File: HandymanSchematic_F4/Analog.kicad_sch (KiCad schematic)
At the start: 36 parts, among them Q1 BC847, U2 TL074, U6 TL072

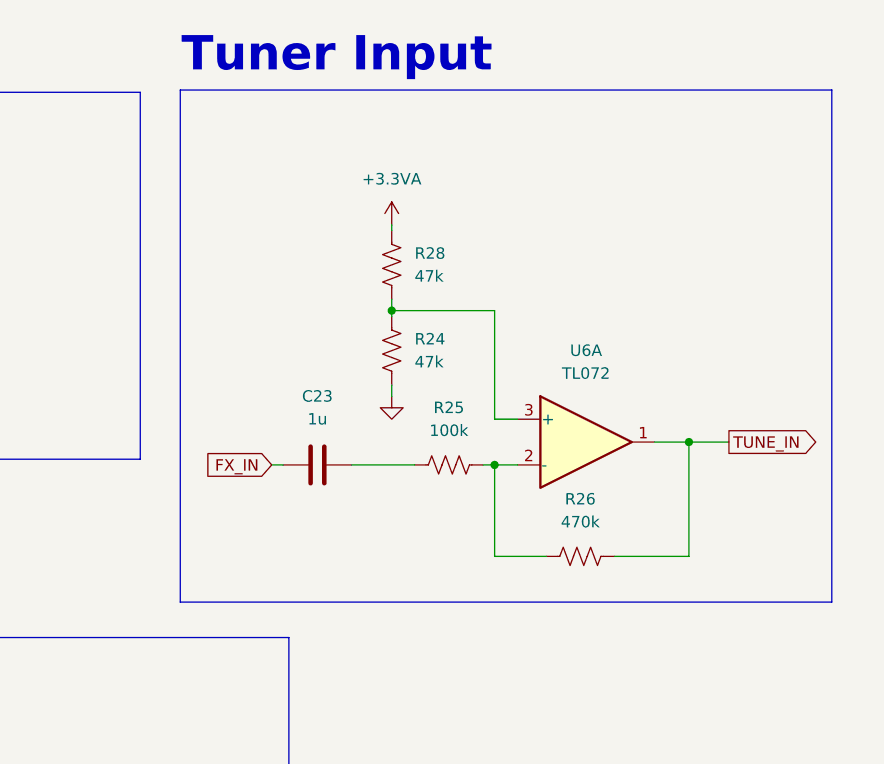
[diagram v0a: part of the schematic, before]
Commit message: schematic changes for DFM
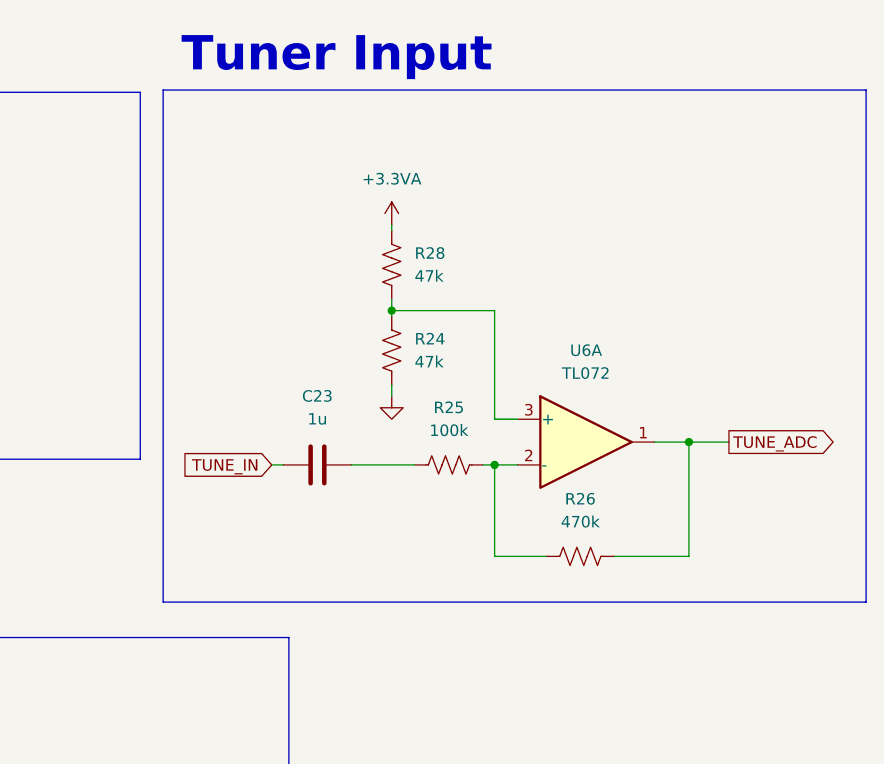
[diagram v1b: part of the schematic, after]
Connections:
- net FX_IN is gone; now on net TUNE_IN: C23.1
- net TUNE_IN: no longer R26.2, U6.1
- new net TUNE_ADC: R26.2, U6.1
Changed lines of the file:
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@@
 	)
 	(rectangle
-		(start 188.595 20.574)
-		(end 260.985 77.47)
+		(start 186.69 20.574)
+		(end 264.795 77.47)
 		(stroke
 			(width 0)
@@
 		)
 	)
-	(global_label "TUNE_IN"
+	(global_label "TUNE_ADC"
 		(shape output)
 		(at 249.555 59.69 0)
@@
 		)
 		(property "Intersheetrefs" "${INTERSHEET_REFS}"
-			(at 260.2207 59.69 0)
+			(at 261.914 59.69 0)
 			(hide yes)
 			(show_name no)
@@
 		)
 	)
-	(global_label "FX_IN"
+	(global_label "TUNE_IN"
 		(shape input)
 		(at 198.755 62.23 180)
@@
 		)
 		(property "Intersheetrefs" "${INTERSHEET_REFS}"
-			(at 190.5688 62.23 0)
+			(at 188.0893 62.23 0)
 			(hide yes)
 			(show_name no)

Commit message: set up BOM w supplier links fixing merge conflict
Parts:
- C1, C3, C4: MPN (none) -> KGF21BR71H104KT; Purchase Link (none) -> https://www.mouser.com/en/ProductDetail/KYOCERA-AVX/KGF21BR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
- C10, C23, C6: MPN (none) -> KGM21AR51E105KU; Purchase Link (none) -> https://www.mouser.com/en/ProductDetail/KYOCERA-AVX/KGM21AR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
- C11: MPN (none) -> KGM21NR71H472JM; Purchase Link (none) -> https://www.mouser.com/en/ProductDetail/KYOCERA-AVX/KGM21NR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
- D1, D4, D5, D6, D7: MPN (none) -> 1N4148W-7-F; Purchase Link (none) -> https://www.mouser.com/en/ProductDetail/Diodes-Incorporated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
- Q1: MPN (none) -> BC847C-C; Purchase Link (none) -> https://www.mouser.com/en/ProductDetail/Diotec-Semiconducto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
- R1, R10, R2, R24, R28, R5, R7: MPN (none) -> RK73B2ATTE473J; Purchase Link (none) -> https://www.mouser.com/en/ProductDetail/KOA-Speer/RK73B2ATT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
- R12, R13, R18, R21, R26, R8: MPN (none) -> AC0805JR-07470KL; Purchase Link (none) -> https://www.mouser.com/en/ProductDetail/YAGEO/AC0805JR-0747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
- R15, R19: MPN (none) -> RT0805FRE0751KL; Purchase Link (none) -> https://www.mouser.com/en/ProductDetail/YAGEO/RT0805FRE0751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
- R22, R25, R9: MPN (none) -> RC0805FR-10100KL; Purchase Link (none) -> https://www.mouser.com/en/ProductDetail/YAGEO/RC0805FR-1010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
- R3: MPN (none) -> AC0805JR-0710KL; Purchase Link (none) -> https://www.mouser.com/en/ProductDetail/YAGEO/AC0805JR-0710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
- RV1, RV2: MPN (none) -> RV9022NO-PA30B7.0-B10K-000-W3.0; Purchase Link (none) -> https://www.taydaelectronics.com/potentiometer-variable-res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
- U2: MPN (none) -> TL074HIDR; Purchase Link (none) -> https://www.mouser.com/en/ProductDetail/Texas-Instruments/T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
- U6: MPN (none) -> TL072HIDR; Purchase Link (none) -> https://www.mouser.com/en/ProductDetail/Texas-Instruments/T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

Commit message: noise schematic tweaks
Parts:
- removed R25: 100k, Resistor_SMD:R_0805_2012Metric, symbol Device:R_US
- removed U6: TL072, Package_SO:SOIC-8_3.9x4.9mm_P1.27mm, symbol Amplifier_Operational:TL072
- added C2, C9: 10u, Capacitor_SMD:C_0805_2012Metric, symbol Device:C
- added C25: 2n2, Capacitor_SMD:C_0805_2012Metric, symbol Device:C
- added D2: BAT54S, Package_TO_SOT_SMD:SOT-23, symbol Diode:BAT54S
- added R11, R4, R6: 220, Resistor_SMD:R_0805_2012Metric, symbol Device:R_US
- added R30: 1Meg, Resistor_SMD:R_0805_2012Metric, symbol Device:R_US
- added R38: 470k, Resistor_SMD:R_0805_2012Metric, symbol Device:R_US
- added R39: 4k7, Resistor_SMD:R_0805_2012Metric, symbol Device:R_US
- added U5: LM2904, Package_SO:SOIC-8_3.9x4.9mm_P1.27mm, symbol Amplifier_Operational:LM2904
- R12, R8: value 470k -> 1Meg
- R13, R26: value 470k -> 100k
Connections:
- net +3.3VA: now also D2.2 (K)
- net AmpAnode: now also R4.2; no longer D7.2 (A)
- net AmpCathode: now also R6.1; no longer D4.1 (K)
- net GND: now also C2.2, C25.2, C9.2, D2.1 (A), U5.4 (V-)
- net TUNE_ADC: now also C25.1, D2.3 (COM), R39.2; no longer R26.2
- net VG: now also U5.6 (-), U5.7
- net at R26.1: now also R38.2, U5.2 (-)
- net at R24.1, R28.2: now also C2.1, R30.2, R38.1
- net at R1.2, R2.1: now also C9.1, U5.5 (+)
- net at C23.2: now also R30.1, U5.3 (+)
- net at R22.2, U2.8: now also R11.1; no longer C10.1
- net +9V renamed +9VA
- net +9VA: now also U5.8 (V+)
- new net: D4.1 (K), R6.2
- new net: D7.2 (A), R4.1
- new net: C10.1, R11.2
- new net: R26.2, R39.1, U5.1
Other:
- moved on the sheet: C1, C10, C11, C23, C3, C6, D4, D5, D6, D7, R1, R10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

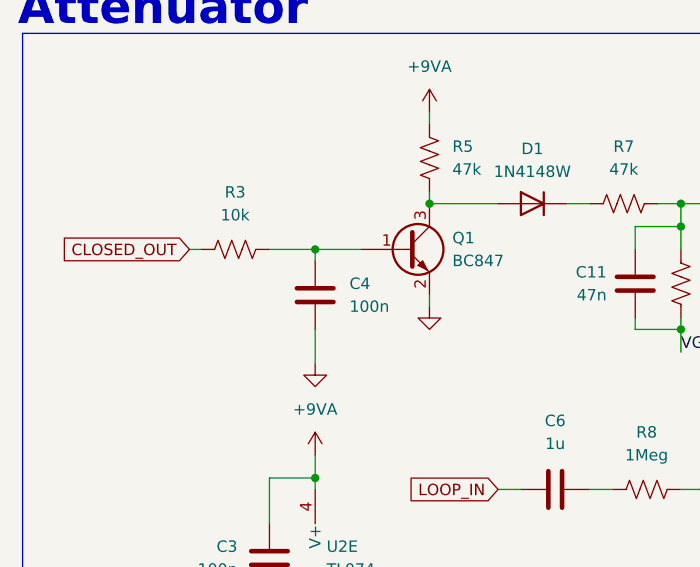
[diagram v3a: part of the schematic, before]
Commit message: switched to FET controlled gate circuit
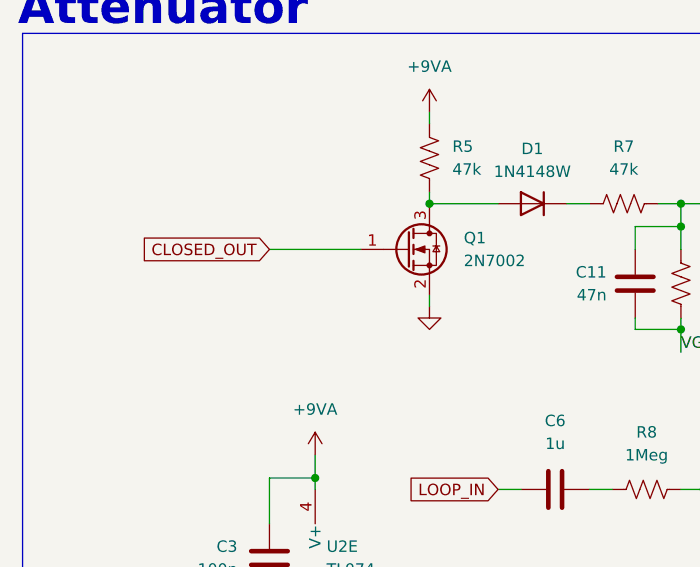
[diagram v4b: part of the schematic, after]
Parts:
- removed C4: 100n, Capacitor_SMD:C_0805_2012Metric, symbol Device:C
- removed Q1: BC847, Package_TO_SOT_SMD:SOT-23, symbol Transistor_BJT:BC847
- removed R3: 10k, Resistor_SMD:R_0805_2012Metric, symbol Device:R_US
- added Q1: 2N7002, Package_TO_SOT_SMD:SOT-23, symbol Transistor_FET:2N7002
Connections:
- net CLOSED_OUT: now also Q1.1 (G)
- net GND: now also Q1.2 (S)
- net at D1.2 (A), R5.2: now also Q1.3 (D)

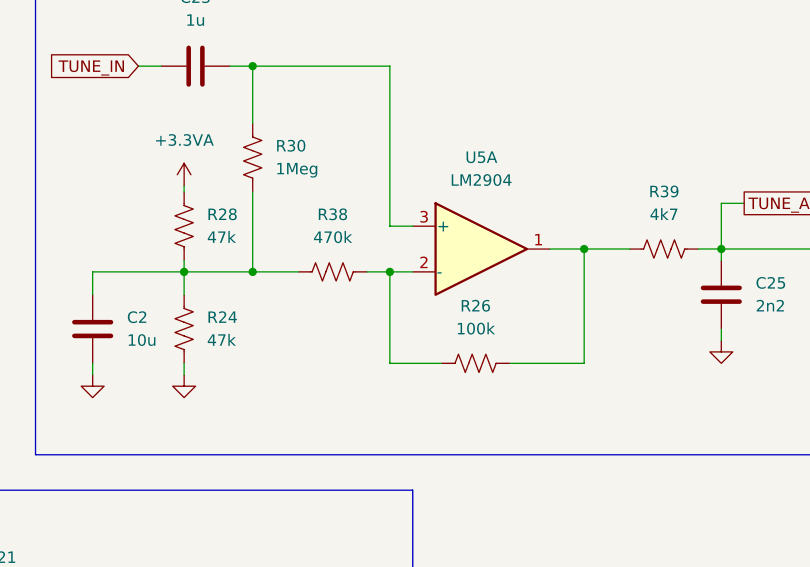
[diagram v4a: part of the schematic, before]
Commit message: fixed hysteresis
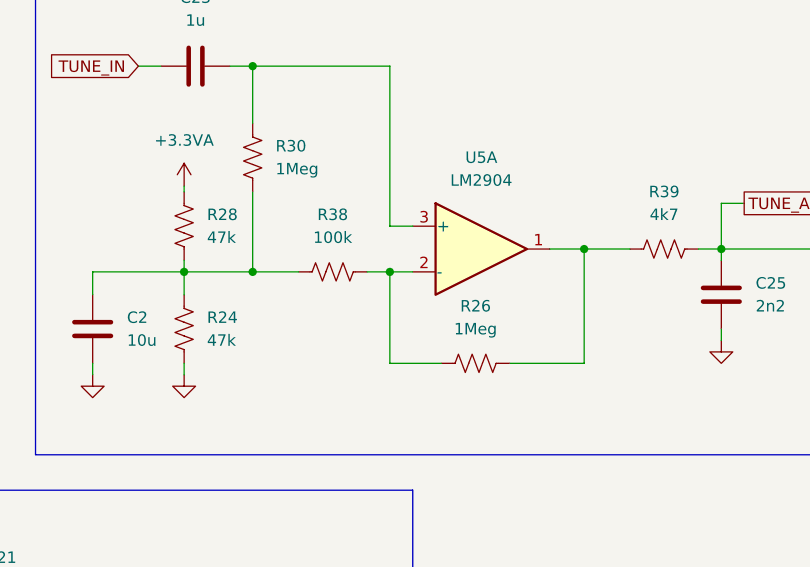
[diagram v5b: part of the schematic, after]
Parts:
- R26: value 100k -> 1Meg
- R38: value 470k -> 100k
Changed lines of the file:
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@@
 			)
 		)
-		(property "Value" "470k"
+		(property "Value" "100k"
 			(at 191.77 53.34 90)
 			(show_name no)
@@
 			)
 		)
-		(property "Value" "100k"
+		(property "Value" "1Meg"
 			(at 207.645 63.5 90)
 			(show_name no)
